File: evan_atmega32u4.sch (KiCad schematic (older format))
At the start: 35 parts, among them J1 USB_B_Mini, J2 AVR-ISP-6, J3 Conn_01x02, J4 Conn_01x03, J5 Conn_01x04, U1 ATmega32U4-AU, Y1 Crystal_Small

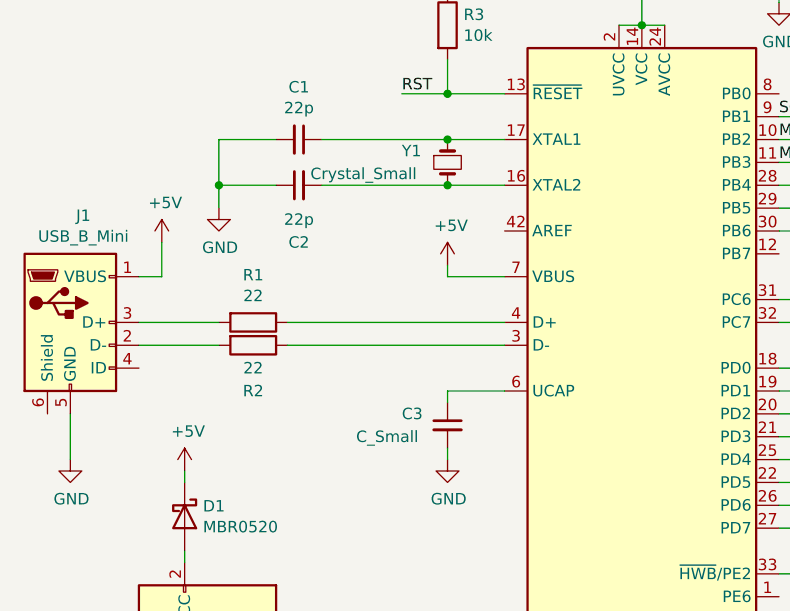
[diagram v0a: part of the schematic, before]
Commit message: update cap value
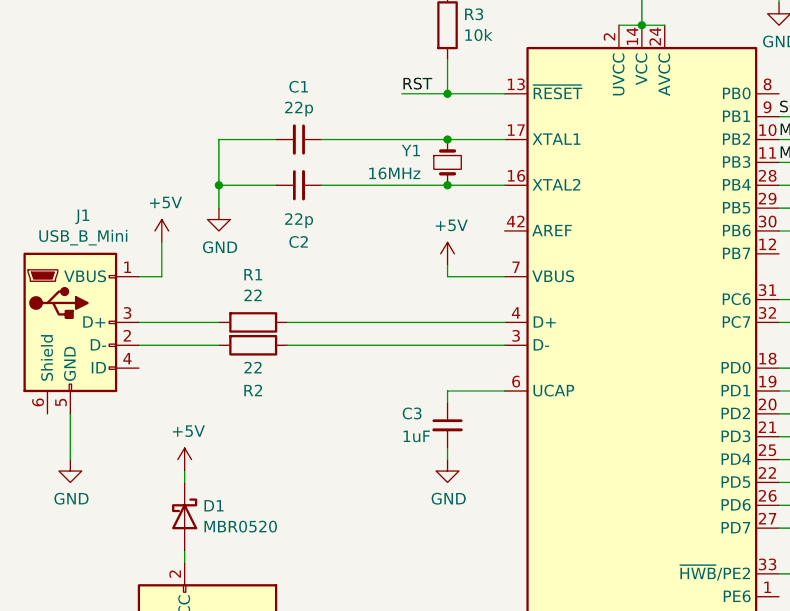
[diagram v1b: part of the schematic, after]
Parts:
- C3: value C_Small -> 1uF
- Y1: value Crystal_Small -> 16MHz
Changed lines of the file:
@@
 P 3700 2200
 F 0 "Y1" V 3650 2000 50  0000 L CNN
-F 1 "Crystal_Small" V 3750 1600 50  0000 L CNN
+F 1 "16MHz" V 3750 1850 50  0000 L CNN
 F 2 "Crystal:Crystal_HC49-U_Vertical" H 3700 2200 50  0001 C CNN
 F 3 "~" H 3700 2200 50  0001 C CNN
@@
 P 3700 3350
 F 0 "C3" H 3500 3400 50  0000 L CNN
-F 1 "C_Small" H 3300 3300 50  0000 L CNN
+F 1 "1uF" H 3500 3300 50  0000 L CNN
 F 2 "Capacitor_SMD:C_0805_2012Metric_Pad1.18x1.45mm_HandSolder" H 3700 3350 50  0001 C CNN
 F 3 "~" H 3700 3350 50  0001 C CNN
